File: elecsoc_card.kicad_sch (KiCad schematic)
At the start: 31 parts, among them J1 Conn_01x02_Pin, J2 Conn_01x02_Pin, U1 NA555D

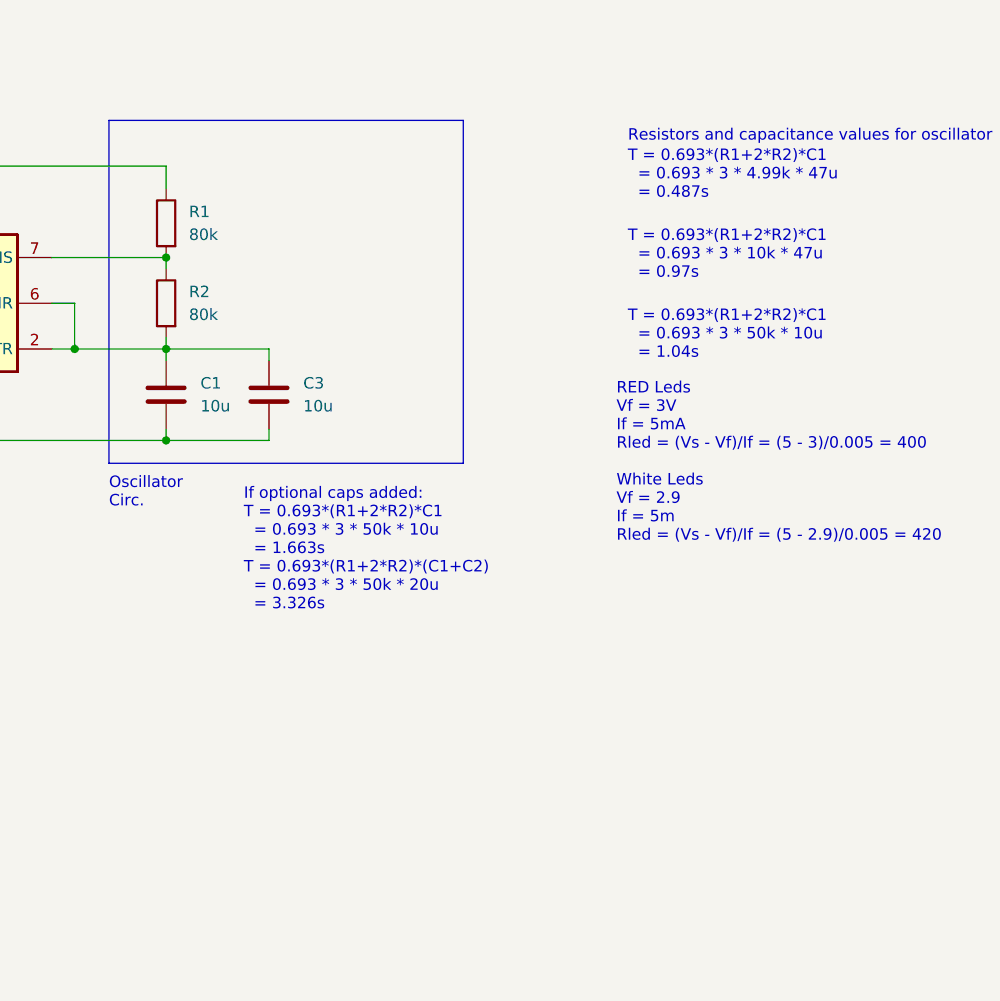
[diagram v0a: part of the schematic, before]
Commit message: Added parallel resistors to change RC constant
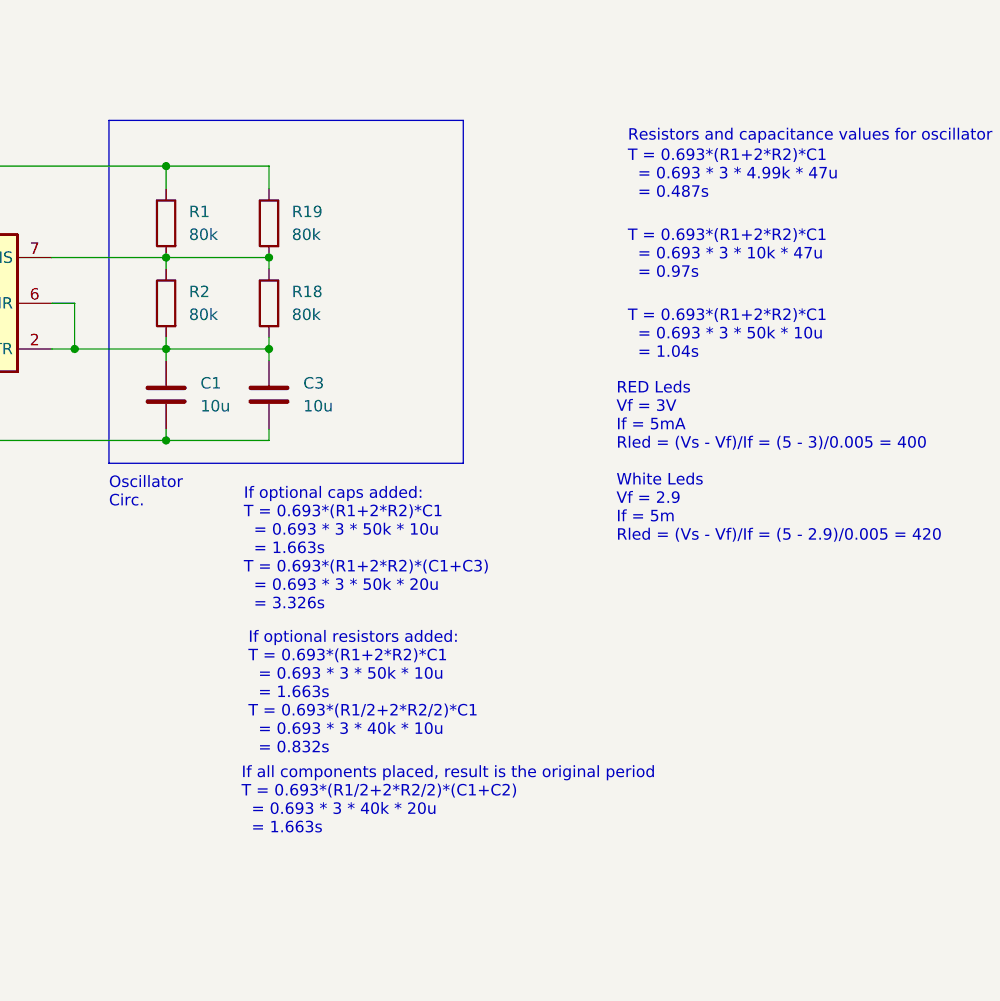
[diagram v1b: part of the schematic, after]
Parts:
- added R18, R19: 80k, Resistor_SMD:R_0805_2012Metric_Pad1.20x1.40mm_HandSolder, symbol Device:R
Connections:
- net +5V: now also R19.1
- net at C1.1, C3.1, R2.2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: now also R18.2
- net at R1.2, R2.1, U1.7 (DIS): now also R18.1, R19.2
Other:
- note added: "If all components placed, result is the original period T = 0.693*(R1/2+2*R2/2)*(C1+C2) = 0.693 * 3 * 40k * 20u = 1.663s"
- note added: "If optional caps added: T = 0.693*(R1+2*R2)*C1 = 0.693 * 3 * 50k * 10u = 1.663s T = 0.693*(R1+2*R2)*(C1+C3) = 0.693 * 3 * 50k * 20u = 3.326s"
- note added: "If optional resistors added: T = 0.693*(R1+2*R2)*C1 = 0.693 * 3 * 50k * 10u = 1.663s T = 0.693*(R1/2+2*R2/2)*C1 = 0.693 * 3 * 40k * 10u = 0.832s"
- note removed: "If optional caps added: T = 0.693*(R1+2*R2)*C1 = 0.693 * 3 * 50k * 10u = 1.663s T = 0.693*(R1+2*R2)*(C1+C2) = 0.693 * 3 * 50k * 20u = 3.326s"
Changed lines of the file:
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@@
 	)
 	(junction
+		(at 193.04 86.36)
+		(diameter 0)
+		(color 0 0 0 0)
+	)
+	(junction
+		(at 181.61 76.2)
+		(diameter 0)
+		(color 0 0 0 0)
+	)
+	(junction
 		(at 111.76 91.44)
 		(diameter 0)
@@
 	)
 	(junction
+		(at 193.04 96.52)
+		(diameter 0)
+		(color 0 0 0 0)
+	)
+	(junction
 		(at 93.98 91.44)
 		(diameter 0)
@@
 	(wire
 		(pts
+			(xy 193.04 86.36) (xy 193.04 87.63)
+		)
+		(stroke
+			(width 0)
+			(type default)
+		)
+	)
+	(wire
+		(pts
 			(xy 181.61 106.68) (xy 193.04 106.68)
 		)
@@
 	(wire
 		(pts
+			(xy 181.61 76.2) (xy 193.04 76.2)
+		)
+		(stroke
+			(width 0)
+			(type default)
+		)
+	)
+	(wire
+		(pts
 			(xy 85.09 74.93) (xy 85.09 78.74)
 		)
@@
 	(wire
 		(pts
+			(xy 181.61 86.36) (xy 193.04 86.36)
+		)
+		(stroke
+			(width 0)
+			(type default)
+		)
+	)
+	(wire
+		(pts
 			(xy 105.41 170.18) (xy 113.03 170.18)
 		)
@@
 	(wire
 		(pts
+			(xy 193.04 95.25) (xy 193.04 96.52)
+		)
+		(stroke
+			(width 0)
+			(type default)
+		)
+	)
+	(wire
+		(pts
 			(xy 120.65 63.5) (xy 111.76 63.5)
 		)
@@
 	(wire
 		(pts
+			(xy 193.04 78.74) (xy 193.04 76.2)
+		)
+		(stroke
+			(width 0)
+			(type default)
+		)
+	)
+	(wire
+		(pts
 			(xy 168.91 86.36) (xy 181.61 86.36)
 		)
@@
 		)
 	)
+	(text "If optional resistors added:\nT = 0.693*(R1+2*R2)*C1\n  = 0.693 * 3 * 50k * 10u \n  = 1.663s\nT = 0.693*(R1/2+2*R2/2)*C1\n  = 0.693 * 3 * 40k * 10u \n  = 0.832s"
+		(exclude_from_sim no)
+		(at 190.754 141.732 0)
+		(effects
+			(font
+				(size 1.27 1.27)
+			)
+			(justify left bottom)
+		)
+	)
 	(text "0603"
 		(exclude_from_sim no)
@@
 		)
 	)
-	(text "If optional caps added:\nT = 0.693*(R1+2*R2)*C1\n  = 0.693 * 3 * 50k * 10u \n  = 1.663s\nT = 0.693*(R1+2*R2)*(C1+C2)\n  = 0.693 * 3 * 50k * 20u \n  = 3.326s"
+	(text "If optional caps added:\nT = 0.693*(R1+2*R2)*C1\n  = 0.693 * 3 * 50k * 10u \n  = 1.663s\nT = 0.693*(R1+2*R2)*(C1+C3)\n  = 0.693 * 3 * 50k * 20u \n  = 3.326s"
 		(exclude_from_sim no)
 		(at 190.246 125.73 0)
@@
 		)
 	)
+	(text "If all components placed, result is the original period\nT = 0.693*(R1/2+2*R2/2)*(C1+C2)\n  = 0.693 * 3 * 40k * 20u \n  = 1.663s"
+		(exclude_from_sim no)
+		(at 189.992 150.622 0)
+		(effects
+			(font
+				(size 1.27 1.27)
+			)
+			(justify left bottom)
+		)
+	)
 	(text "T = 0.693*(R1+2*R2)*C1\n  = 0.693 * 3 * 4.99k * 47u \n  = 0.487s"
 		(exclude_from_sim no)
@@
 	)
 	(symbol
+		(lib_id "Device:R")
+		(at 193.04 82.55 0)
+		(mirror y)
+		(unit 1)
+		(exclude_from_sim no)
+		(in_bom yes)
+		(on_board yes)
+		(dnp no)
+		(fields_autoplaced yes)
+		(property "Reference" "R19"
+			(at 195.58 81.28 0)
+			(effects
+				(font
+					(size 1.27 1.27)
+				)
+				(justify right)
+			)
+		)
+		(property "Value" "80k"
+			(at 195.58 83.82 0)
+			(effects
+				(font
+					(size 1.27 1.27)
+				)
+				(justify right)
+			)
+		)
+		(property "Footprint" "Resistor_SMD:R_0805_2012Metric_Pad1.20x1.40mm_HandSolder"
+			(at 194.818 82.55 90)
+			(effects
+				(font
+					(size 1.27 1.27)
+				)
+				(hide yes)
+			)
+		)
+		(property "Datasheet" "~"
+			(at 193.04 82.55 0)
+			(effects
+				(font
+					(size 1.27 1.27)
+				)
+				(hide yes)
+			)
+		)
+		(property "Description" ""
+			(at 193.04 82.55 0)
+			(effects
+				(font
+					(size 1.27 1.27)
+				)
+				(hide yes)
+			)
+		)
+		(pin "1"
+		)
+		(pin "2"
+		)
+		(instances
+			(project "elecsoc_card"
+				(path "/ec1e128b-e85b-4f54-a1e1-536be465431f"
+					(reference "R19")
+					(unit 1)
+				)
+			)
+		)
+	)
+	(symbol
 		(lib_id "power:GND")
 		(at 64.77 176.53 0)
@@
 					(unit 1)
 				)
+			)
+		)
+	)
+	(symbol
+		(lib_id "Device:R")
+		(at 193.04 91.44 0)
+		(mirror y)
+		(unit 1)
+		(exclude_from_sim no)
+		(in_bom yes)
+		(on_board yes)
+		(dnp no)
+		(fields_autoplaced yes)
+		(property "Reference" "R18"
+			(at 195.58 90.17 0)
+			(effects
+				(font
+					(size 1.27 1.27)
+				)
+				(justify right)
+			)
+		)
+		(property "Value" "80k"
+			(at 195.58 92.71 0)
+			(effects
+				(font
+					(size 1.27 1.27)
+				)
+				(justify right)
+			)
+		)
+		(property "Footprint" "Resistor_SMD:R_0805_2012Metric_Pad1.20x1.40mm_HandSolder"
+			(at 194.818 91.44 90)
+			(effects
+				(font
+					(size 1.27 1.27)
+				)
+				(hide yes)
+			)
+		)
+		(property "Datasheet" "~"
+			(at 193.04 91.44 0)
+			(effects
+				(font
+					(size 1.27 1.27)
+				)
+				(hide yes)
+			)
+		)
+		(property "Description" ""
+			(at 193.04 91.44 0)
+			(effects
+				(font
+					(size 1.27 1.27)
+				)
+				(hide yes)
+			)
+		)
+		(pin "1"
+		)
+		(pin "2"
+		)
+		(instances
+			(project "elecsoc_card"
+				(path "/ec1e128b-e85b-4f54-a1e1-536be465431f"
+					(reference "R18")
+					(unit 1)
+				)

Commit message: Values corrected
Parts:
- R1, R18, R19, R2: value 80k -> 50k
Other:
- note added: "If all components placed, result is the original period T = 0.693*(R1/2+2*R2/2)*(C1+C2) = 0.693 * 3 * 25k * 10u = 1.04s"
- note added: "If optional caps added: T = 0.693*(R1+2*R2)*C1 = 0.693 * 3 * 50k * 10u = 1.04s T = 0.693*(R1+2*R2)*(C1+C3) = 0.693 * 3 * 50k * 20u = 2.079s"
- note added: "If optional resistors added: T = 0.693*(R1+2*R2)*C1 = 0.693 * 3 * 50k * 10u = 1.04s T = 0.693*(R1/2+2*R2/2)*C1 = 0.693 * 3 * 25k * 10u = 0.52s"
- note added: "Optional"
- note removed: "If all components placed, result is the original period T = 0.693*(R1/2+2*R2/2)*(C1+C2) = 0.693 * 3 * 40k * 20u = 1.663s"
- note removed: "If optional caps added: T = 0.693*(R1+2*R2)*C1 = 0.693 * 3 * 50k * 10u = 1.663s T = 0.693*(R1+2*R2)*(C1+C3) = 0.693 * 3 * 50k * 20u = 3.326s"
- note removed: "If optional resistors added: T = 0.693*(R1+2*R2)*C1 = 0.693 * 3 * 50k * 10u = 1.663s T = 0.693*(R1/2+2*R2/2)*C1 = 0.693 * 3 * 40k * 10u = 0.832s"
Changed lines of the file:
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@@
 	)
 	(rectangle
+		(start 190.5 74.93)
+		(end 201.93 107.95)
+		(stroke
+			(width 0)
+			(type default)
+		)
+		(fill
+			(type none)
+		)
+	)
+	(rectangle
 		(start 214.63 21.59)
 		(end 259.08 46.99)
@@
 		)
 	)
-	(text "If optional resistors added:\nT = 0.693*(R1+2*R2)*C1\n  = 0.693 * 3 * 50k * 10u \n  = 1.663s\nT = 0.693*(R1/2+2*R2/2)*C1\n  = 0.693 * 3 * 40k * 10u \n  = 0.832s"
+	(text "If optional resistors added:\nT = 0.693*(R1+2*R2)*C1\n  = 0.693 * 3 * 50k * 10u \n  = 1.04s\nT = 0.693*(R1/2+2*R2/2)*C1\n  = 0.693 * 3 * 25k * 10u \n  = 0.52s"
 		(exclude_from_sim no)
 		(at 190.754 141.732 0)
@@
 		)
 	)
-	(text "If optional caps added:\nT = 0.693*(R1+2*R2)*C1\n  = 0.693 * 3 * 50k * 10u \n  = 1.663s\nT = 0.693*(R1+2*R2)*(C1+C3)\n  = 0.693 * 3 * 50k * 20u \n  = 3.326s"
+	(text "If optional caps added:\nT = 0.693*(R1+2*R2)*C1\n  = 0.693 * 3 * 50k * 10u \n  = 1.04s\nT = 0.693*(R1+2*R2)*(C1+C3)\n  = 0.693 * 3 * 50k * 20u \n  = 2.079s"
 		(exclude_from_sim no)
 		(at 190.246 125.73 0)
@@
 		)
 	)
-	(text "If all components placed, result is the original period\nT = 0.693*(R1/2+2*R2/2)*(C1+C2)\n  = 0.693 * 3 * 40k * 20u \n  = 1.663s"
+	(text "If all components placed, result is the original period\nT = 0.693*(R1/2+2*R2/2)*(C1+C2)\n  = 0.693 * 3 * 25k * 10u \n  = 1.04s"
 		(exclude_from_sim no)
 		(at 189.992 150.622 0)
@@
 		)
 	)
+	(text "Optional"
+		(exclude_from_sim no)
+		(at 192.532 74.168 0)
+		(effects
+			(font
+				(size 1.27 1.27)
+			)
+			(justify left bottom)
+		)
+	)
 	(text "T = 0.693*(R1+2*R2)*C1\n  = 0.693 * 3 * 4.99k * 47u \n  = 0.487s"
 		(exclude_from_sim no)
@@
 		(fields_autoplaced yes)
 		(property "Reference" "R19"
-			(at 195.58 81.28 0)
+			(at 195.58 81.2799 0)
 			(effects
 				(font
@@
 			)
 		)
-		(property "Value" "80k"
-			(at 195.58 83.82 0)
+		(property "Value" "50k"
+			(at 195.58 83.8199 0)
 			(effects
 				(font
@@
 		(fields_autoplaced yes)
 		(property "Reference" "R2"
-			(at 184.15 90.17 0)
+			(at 184.15 90.1699 0)
 			(effects
 				(font
@@
 			)
 		)
-		(property "Value" "80k"
-			(at 184.15 92.71 0)
+		(property "Value" "50k"
+			(at 184.15 92.7099 0)
 			(effects
 				(font
@@
 		(fields_autoplaced yes)
 		(property "Reference" "R1"
-			(at 184.15 81.28 0)
+			(at 184.15 81.2799 0)
 			(effects
 				(font
@@
 			)
 		)
-		(property "Value" "80k"
-			(at 184.15 83.82 0)
+		(property "Value" "50k"
+			(at 184.15 83.8199 0)
 			(effects
 				(font
@@
 		(fields_autoplaced yes)
 		(property "Reference" "R18"
-			(at 195.58 90.17 0)
+			(at 195.58 90.1699 0)
 			(effects
 				(font
@@
 			)
 		)
-		(property "Value" "80k"
-			(at 195.58 92.71 0)
+		(property "Value" "50k"
+			(at 195.58 92.7099 0)
 			(effects
 				(font

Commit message: Back to 80k
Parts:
- R1, R18, R19, R2: value 50k -> 80k
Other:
- note added: "If all components placed, result is the original period T = 0.693*(R1/2+2*R2/2)*(C1+C2) = 0.693 * 3 * 40k * 20u = 1.663s"
- note added: "If optional caps added: T = 0.693*(R1+2*R2)*C1 = 0.693 * 3 * 50k * 10u = 1.663s T = 0.693*(R1+2*R2)*(C1+C3) = 0.693 * 3 * 50k * 20u = 3.326s"
- note added: "If optional resistors added: T = 0.693*(R1+2*R2)*C1 = 0.693 * 3 * 50k * 10u = 1.663s T = 0.693*(R1/2+2*R2/2)*C1 = 0.693 * 3 * 40k * 10u = 0.832s"
- note removed: "If all components placed, result is the original period T = 0.693*(R1/2+2*R2/2)*(C1+C2) = 0.693 * 3 * 25k * 10u = 1.04s"
- note removed: "If optional caps added: T = 0.693*(R1+2*R2)*C1 = 0.693 * 3 * 50k * 10u = 1.04s T = 0.693*(R1+2*R2)*(C1+C3) = 0.693 * 3 * 50k * 20u = 2.079s"
- note removed: "If optional resistors added: T = 0.693*(R1+2*R2)*C1 = 0.693 * 3 * 50k * 10u = 1.04s T = 0.693*(R1/2+2*R2/2)*C1 = 0.693 * 3 * 25k * 10u = 0.52s"
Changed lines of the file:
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@@
 		)
 	)
-	(text "If optional resistors added:\nT = 0.693*(R1+2*R2)*C1\n  = 0.693 * 3 * 50k * 10u \n  = 1.04s\nT = 0.693*(R1/2+2*R2/2)*C1\n  = 0.693 * 3 * 25k * 10u \n  = 0.52s"
+	(text "If optional resistors added:\nT = 0.693*(R1+2*R2)*C1\n  = 0.693 * 3 * 50k * 10u \n  = 1.663s\nT = 0.693*(R1/2+2*R2/2)*C1\n  = 0.693 * 3 * 40k * 10u \n  = 0.832s"
 		(exclude_from_sim no)
 		(at 190.754 141.732 0)
@@
 		)
 	)
-	(text "If optional caps added:\nT = 0.693*(R1+2*R2)*C1\n  = 0.693 * 3 * 50k * 10u \n  = 1.04s\nT = 0.693*(R1+2*R2)*(C1+C3)\n  = 0.693 * 3 * 50k * 20u \n  = 2.079s"
+	(text "If optional caps added:\nT = 0.693*(R1+2*R2)*C1\n  = 0.693 * 3 * 50k * 10u \n  = 1.663s\nT = 0.693*(R1+2*R2)*(C1+C3)\n  = 0.693 * 3 * 50k * 20u \n  = 3.326s"
 		(exclude_from_sim no)
 		(at 190.246 125.73 0)
@@
 		)
 	)
-	(text "If all components placed, result is the original period\nT = 0.693*(R1/2+2*R2/2)*(C1+C2)\n  = 0.693 * 3 * 25k * 10u \n  = 1.04s"
+	(text "If all components placed, result is the original period\nT = 0.693*(R1/2+2*R2/2)*(C1+C2)\n  = 0.693 * 3 * 40k * 20u \n  = 1.663s"
 		(exclude_from_sim no)
 		(at 189.992 150.622 0)
@@
 			)
 		)
-		(property "Value" "50k"
+		(property "Value" "80k"
 			(at 195.58 83.8199 0)
 			(effects
@@
 			)
 		)
-		(property "Value" "50k"
+		(property "Value" "80k"
 			(at 184.15 92.7099 0)
 			(effects
@@
 			)
 		)
-		(property "Value" "50k"
+		(property "Value" "80k"
 			(at 184.15 83.8199 0)
 			(effects
@@
 			)
 		)
-		(property "Value" "50k"
+		(property "Value" "80k"
 			(at 195.58 92.7099 0)
 			(effects
